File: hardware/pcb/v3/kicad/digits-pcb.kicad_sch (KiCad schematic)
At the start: 44 parts, among them J8 Conn_01x04, SW1 Hook_DPDT, SW2 SW_Push, U3 RP2040, U4 W25Q16JVSSIQ, U5 AMS1117-3.3, Y1 ABM8-272-T3

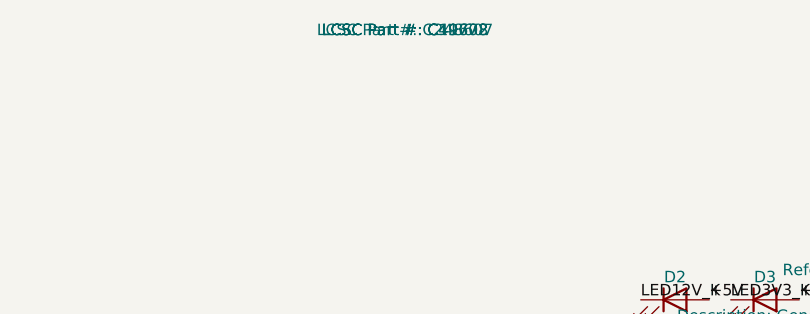
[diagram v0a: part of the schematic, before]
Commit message: chore(hardware): assign LCSC parts to power LEDs and their resistors
D2 (red 0603) C2286, D3 (green 0603) C12624, R12 (300 ohm 0402) C25102,
R13 (330 ohm 0402) C25104. These were added in the power-LED work after
the earlier LCSC pass and had no part assigned. The resistors use the
same UNI-ROYAL 0402WGF series as the existing boost divider. Fields are
added to both symbol and footprint (hidden, F.Fab) so schematic-parity
stays clean and the PCB-based BOM picks them up.
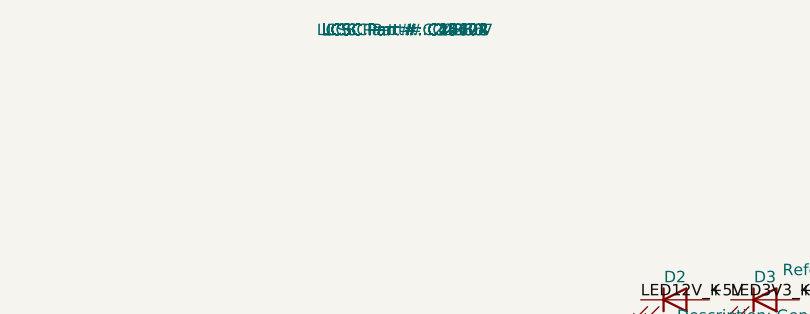
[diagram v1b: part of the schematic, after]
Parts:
- D2: LCSC Part # (none) -> C2286
- D3: LCSC Part # (none) -> C12624
- R12: LCSC Part # (none) -> C25102
- R13: LCSC Part # (none) -> C25104
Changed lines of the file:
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@@
+			)
+		)
+		(property "LCSC Part #" "C25102"
+			(at 0 0 0)
+			(show_name yes)
+			(do_not_autoplace no)
+			(effects
+				(font
+					(size 1.27 1.27)
+				)
 			)
 		)
@@
 			)
 		)
+		(property "LCSC Part #" "C12624"
+			(at 0 0 0)
+			(show_name yes)
+			(do_not_autoplace no)
+			(effects
+				(font
+					(size 1.27 1.27)
+				)
+			)
+		)
 		(pin "1"
 		)
@@
 			)
 		)
+		(property "LCSC Part #" "C2286"
+			(at 0 0 0)
+			(show_name yes)
+			(do_not_autoplace no)
+			(effects
+				(font
+					(size 1.27 1.27)
+				)
+			)
+		)
 		(pin "1"
 		)
@@
 			(do_not_autoplace no)
 			(effects
+				(font
+					(size 1.27 1.27)
+				)
+			)
+		)
+		(property "LCSC Part #" "C25104"
+			(at 0 0 0)
+			(show_name yes)
+			(do_not_autoplace no)
+			(effects

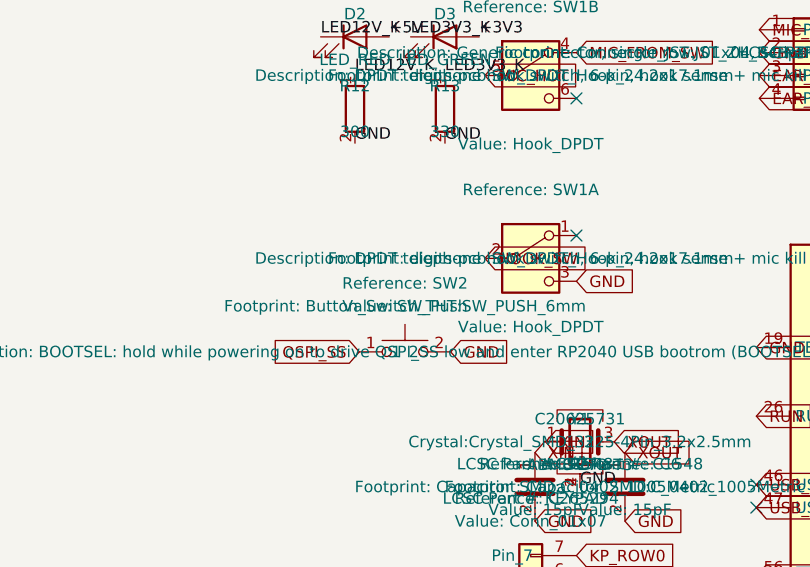
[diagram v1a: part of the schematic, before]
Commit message: fix(hardware): rate C55 for the 37V boost rail, assign SW2 BOOTSEL part
C55 was a 25V electrolytic on VBOOST (37.25V), which would over-volt and
fail. It is local VM decoupling, not the rail source (the XL6019 regulates
37V and C100's 100uF is the bulk reservoir), so dropping it to 10uF/50V
(C116402) in the same 5mm footprint keeps the decoupling ample with no
layout change. Also assign the SW2 6mm tactile (OMRON B3F-1002, C87036)
so the BOOTSEL button places.

DRC stays clean: 0 errors, 0 unconnected, 0 schematic-parity.
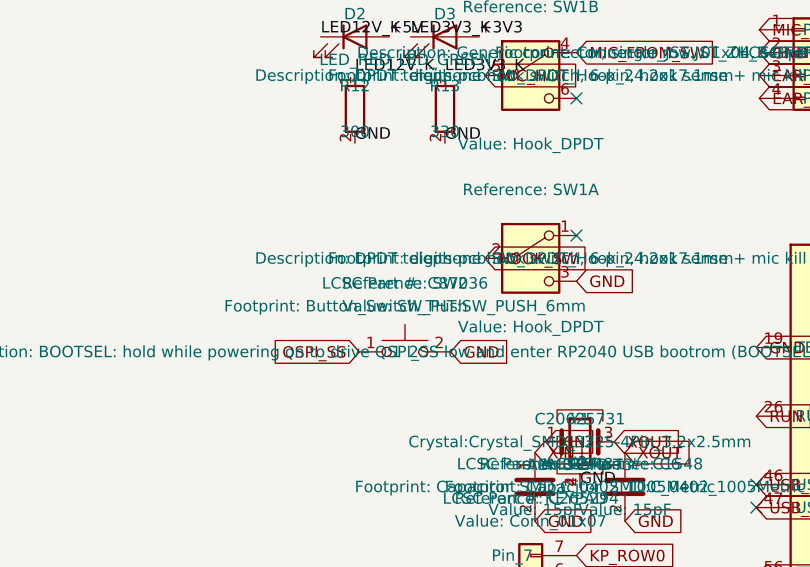
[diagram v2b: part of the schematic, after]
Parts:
- SW2: LCSC Part # (none) -> C87036
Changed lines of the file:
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@@
 			)
 		)
-		(property "LCSC Part #" ""
+		(property "LCSC Part #" "C87036"
 			(at 35.56 57.38 0)
 			(show_name yes)

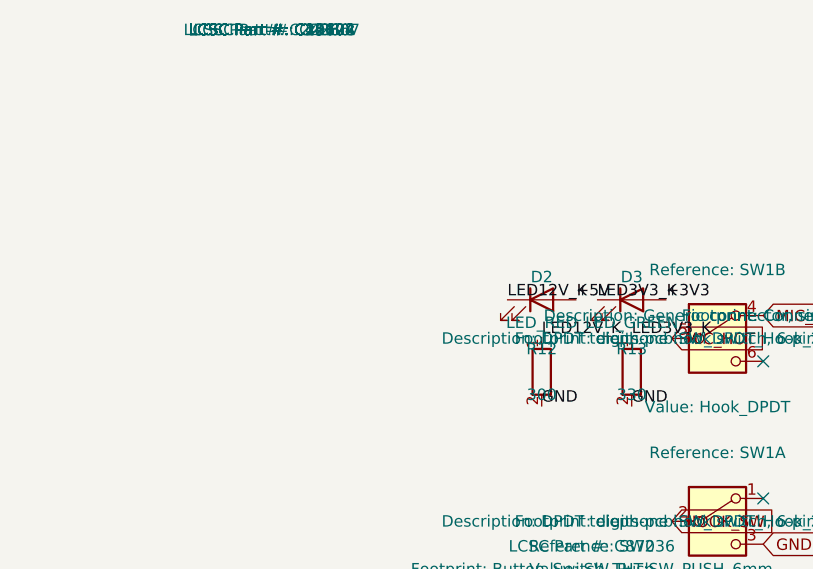
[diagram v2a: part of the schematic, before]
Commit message: fix(hardware): make the +3V3 green indicator reliable (D3, R13)
The emerald-green D3 (Vf ~3.1V) had only ~0.2V of headroom on the 3.3V
rail, so it would barely light and vary part-to-part. Switch to a low-Vf
yellow-green LED (KT-0603YG, C2289) and resize R13 to 120 ohm (C25752)
for ~10mA, matching the +5V red indicator. Same footprints, no re-route.
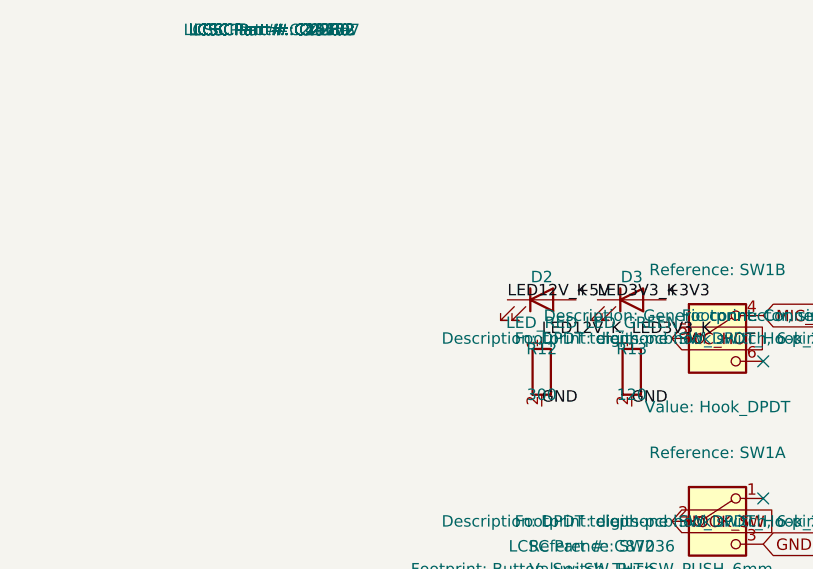
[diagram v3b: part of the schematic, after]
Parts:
- D3: LCSC Part # C12624 -> C2289
- R13: value 330 -> 120; LCSC Part # C25104 -> C25752
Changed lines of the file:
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@@
 			)
 		)
-		(property "LCSC Part #" "C12624"
+		(property "LCSC Part #" "C2289"
 			(at 0 0 0)
 			(show_name yes)
@@
 			)
 		)
-		(property "Value" "330"
+		(property "Value" "120"
 			(at 40 40.54 0)
 			(show_name no)
@@
 			)
 		)
-		(property "LCSC Part #" "C25104"
+		(property "LCSC Part #" "C25752"
 			(at 0 0 0)
 			(show_name yes)

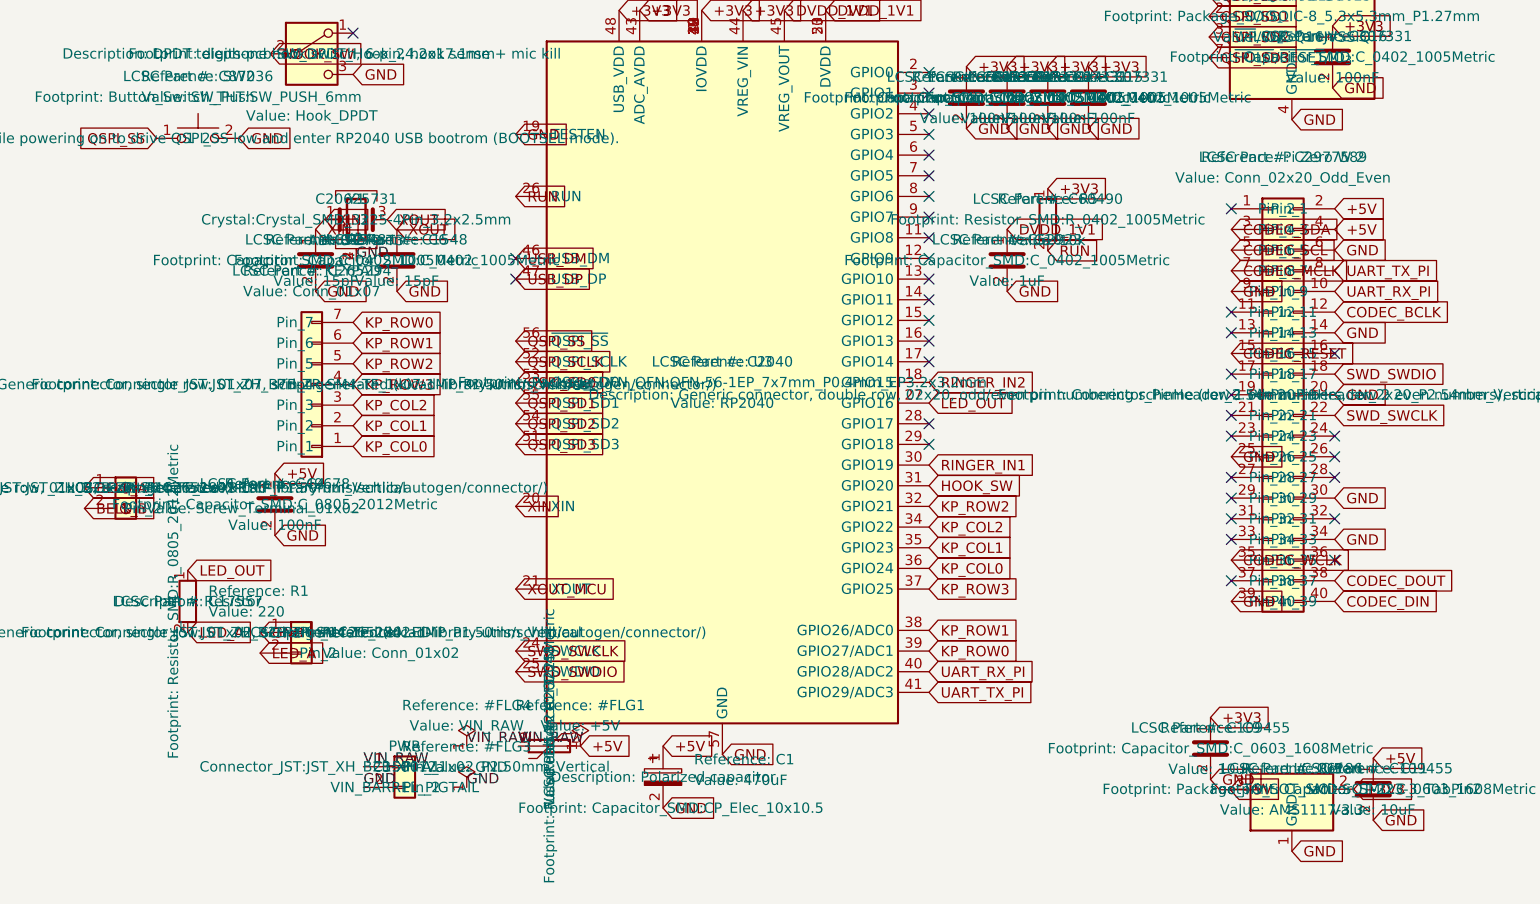
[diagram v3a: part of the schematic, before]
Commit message: fix(hardware): annotate connector refs (PWR1/LED1/etc.) for stable sync
KiCad's annotation during Update-PCB-from-Schematic numbered the un-annotated
semantic refs on the PCB: PWR->PWR1, LED->LED1, KEYPAD->KEYPAD1, BELL->BELL1,
Pi Zero W 2->Pi Zero W1. Sync the schematic and the production BOM to the same
forms so all three agree and schematic-parity is clean. The numbered refs are
valid annotations, so future re-syncs no longer re-mangle them.

DRC: 0 errors, 0 unconnected, 0 schematic-parity.
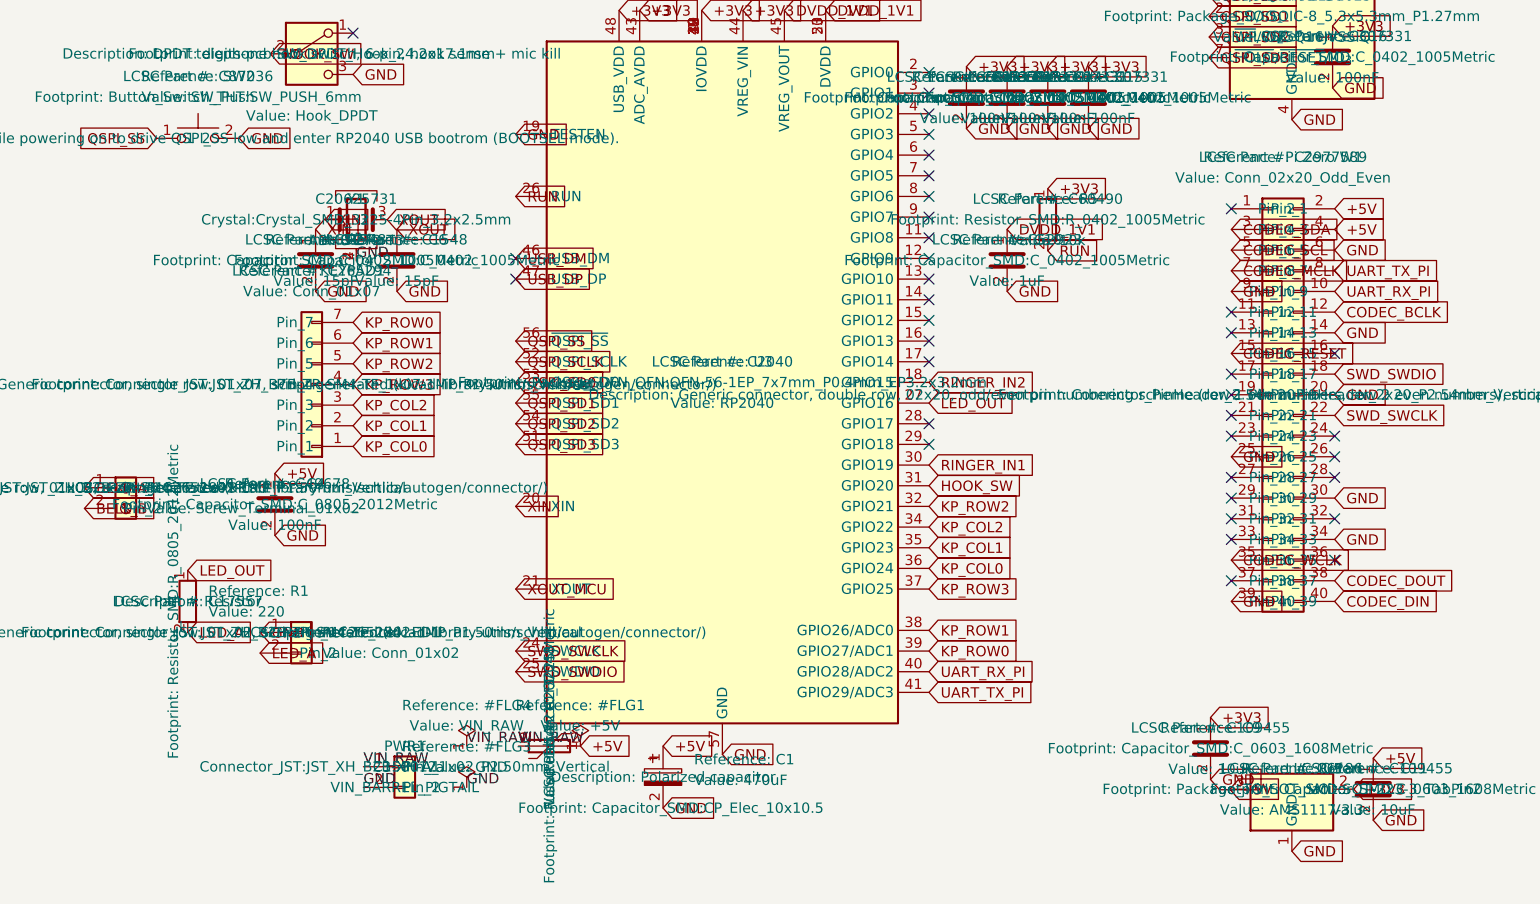
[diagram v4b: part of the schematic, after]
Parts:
- Pi Zero W1: renamed from Pi Zero W 2
- renumbered BELL to BELL1, KEYPAD to KEYPAD1, LED to LED1, PWR to PWR1
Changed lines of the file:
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@@
 		(dnp no)
 		(fields_autoplaced yes)
-		(property "Reference" "BELL"
+		(property "Reference" "BELL1"
 			(at 29.21 107.9499 0)
 			(show_name yes)
@@
 			(project "digits-pcb"
 				(path "/74ec24e7-a8af-4132-928f-b03228b07139"
-					(reference "BELL")
+					(reference "BELL1")
 					(unit 1)
 				)
@@
 		(in_pos_files yes)
 		(dnp no)
-		(property "Reference" "PWR"
+		(property "Reference" "PWR1"
 			(at 60.96 139.7 0)
 			(show_name no)
@@
 			(project "digits-pcb"
 				(path "/74ec24e7-a8af-4132-928f-b03228b07139"
-					(reference "PWR")
+					(reference "PWR1")
 					(unit 1)
 				)
@@
 		(dnp no)
 		(fields_autoplaced yes)
-		(property "Reference" "LED"
+		(property "Reference" "LED1"
 			(at 50.8 125.7299 0)
 			(show_name yes)
@@
 			(project "digits-pcb"
 				(path "/74ec24e7-a8af-4132-928f-b03228b07139"
-					(reference "LED")
+					(reference "LED1")
 					(unit 1)
 				)
@@
 		(dnp no)
 		(fields_autoplaced yes)
-		(property "Reference" "Pi Zero W 2"
+		(property "Reference" "Pi Zero W1"
 			(at 168.91 67.31 0)
 			(show_name yes)
@@
 			(project "digits-pcb"
 				(path "/74ec24e7-a8af-4132-928f-b03228b07139"
-					(reference "Pi Zero W 2")
+					(reference "Pi Zero W1")
 					(unit 1)
 				)
@@
 		(dnp no)
 		(fields_autoplaced yes)
-		(property "Reference" "KEYPAD"
+		(property "Reference" "KEYPAD1"
 			(at 49.53 81.28 0)
 			(show_name yes)
@@
 			(project "digits-pcb"
 				(path "/74ec24e7-a8af-4132-928f-b03228b07139"
-					(reference "KEYPAD")
-					(unit 1)
-				)
+					(reference "KEYPAD1")
+					(unit 1)
+				)

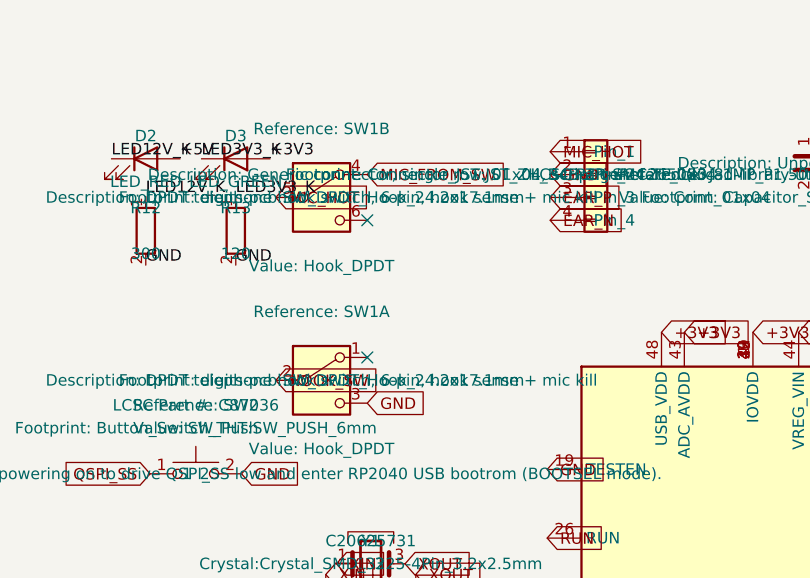
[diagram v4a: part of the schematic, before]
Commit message: fix(hardware): re-pin SW1 to match the physical DPDT pole structure
Bench multimeter showed the hook switch's commons are pins 1 and 4 (not the
middle pins the symbol assumed): rest connects 1+3 and 4+6, pressed connects
1+2 and 4+5. Re-assign the SW1 nets so the real part wires correctly:
pin1=HOOK_SW, pin2=GND, pin4=MIC_HOT, pin6=MIC_FROM_SW, pins 3 and 5 unused.

Pressed (on-hook) now grounds HOOK_SW (matches the firmware default polarity,
no invert) and opens the mic loop; at rest the mic loop closes and the mic is
live. Schematic only; the PCB needs Update-from-Schematic and a reroute of the
four nets to their new pads.
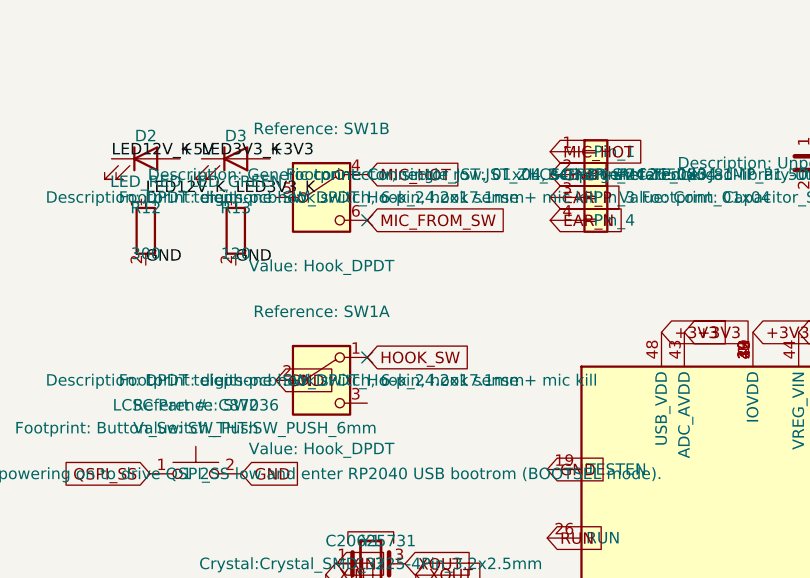
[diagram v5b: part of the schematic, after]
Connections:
- net GND: now also SW1.2 (B); no longer SW1.3 (C)
- net HOOK_SW: now also SW1.1 (A); no longer SW1.2 (B)
- net MIC_FROM_SW: now also SW1.6 (C); no longer SW1.4 (A)
- net MIC_HOT: now also SW1.4 (A); no longer SW1.5 (B)

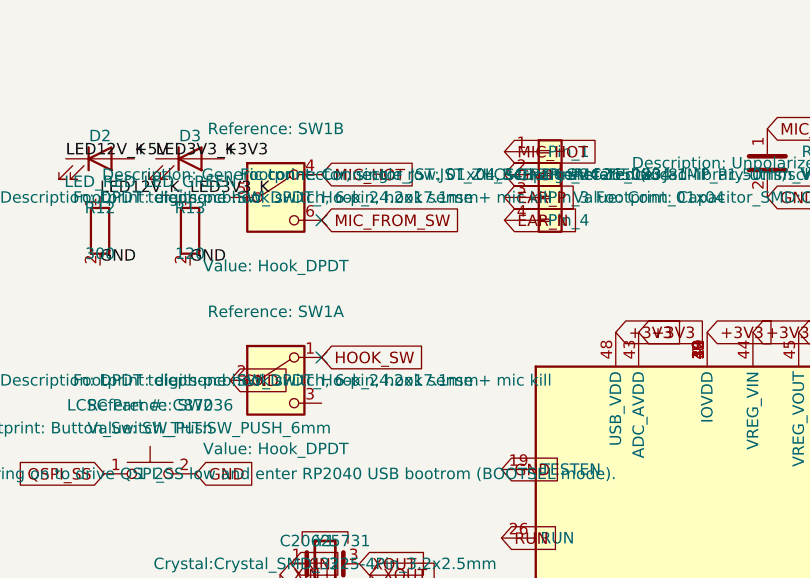
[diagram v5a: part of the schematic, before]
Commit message: fix(hardware): correct SW1 throw orientation (swap pads 1/3 and 4/6)
The back-side mounting mirrors the left/right columns, so the physical
commons (pins 1 and 4) land on footprint pads 3 and 6, not 1 and 4. Swap
the throws within each pole: pad3=HOOK_SW, pad1 unused; pad6=MIC_HOT,
pad4=MIC_FROM_SW (pad2=GND and pad5 unused are unchanged).

Bench-verified pole structure now maps correctly: pressed (on-hook) grounds
HOOK_SW and opens the mic loop; at rest (off-hook) the mic loop is live.
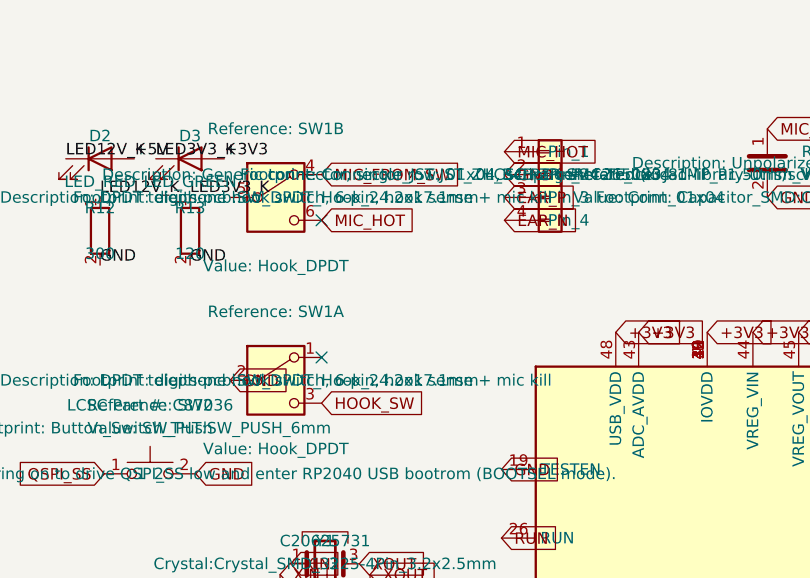
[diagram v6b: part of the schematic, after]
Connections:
- net HOOK_SW: now also SW1.3 (C); no longer SW1.1 (A)
- net MIC_FROM_SW: now also SW1.4 (A); no longer SW1.6 (C)
- net MIC_HOT: now also SW1.6 (C); no longer SW1.4 (A)
